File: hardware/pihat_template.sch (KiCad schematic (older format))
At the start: 29 parts, among them P1 CONN_01X02, P2 CONN_01X02, P3 Raspberry_Pi_+_Conn, U1 LM3489, U2 CAT24C32HU4I-GT3, U3 FDC5614P, U4 LM1117IMPX-ADJ

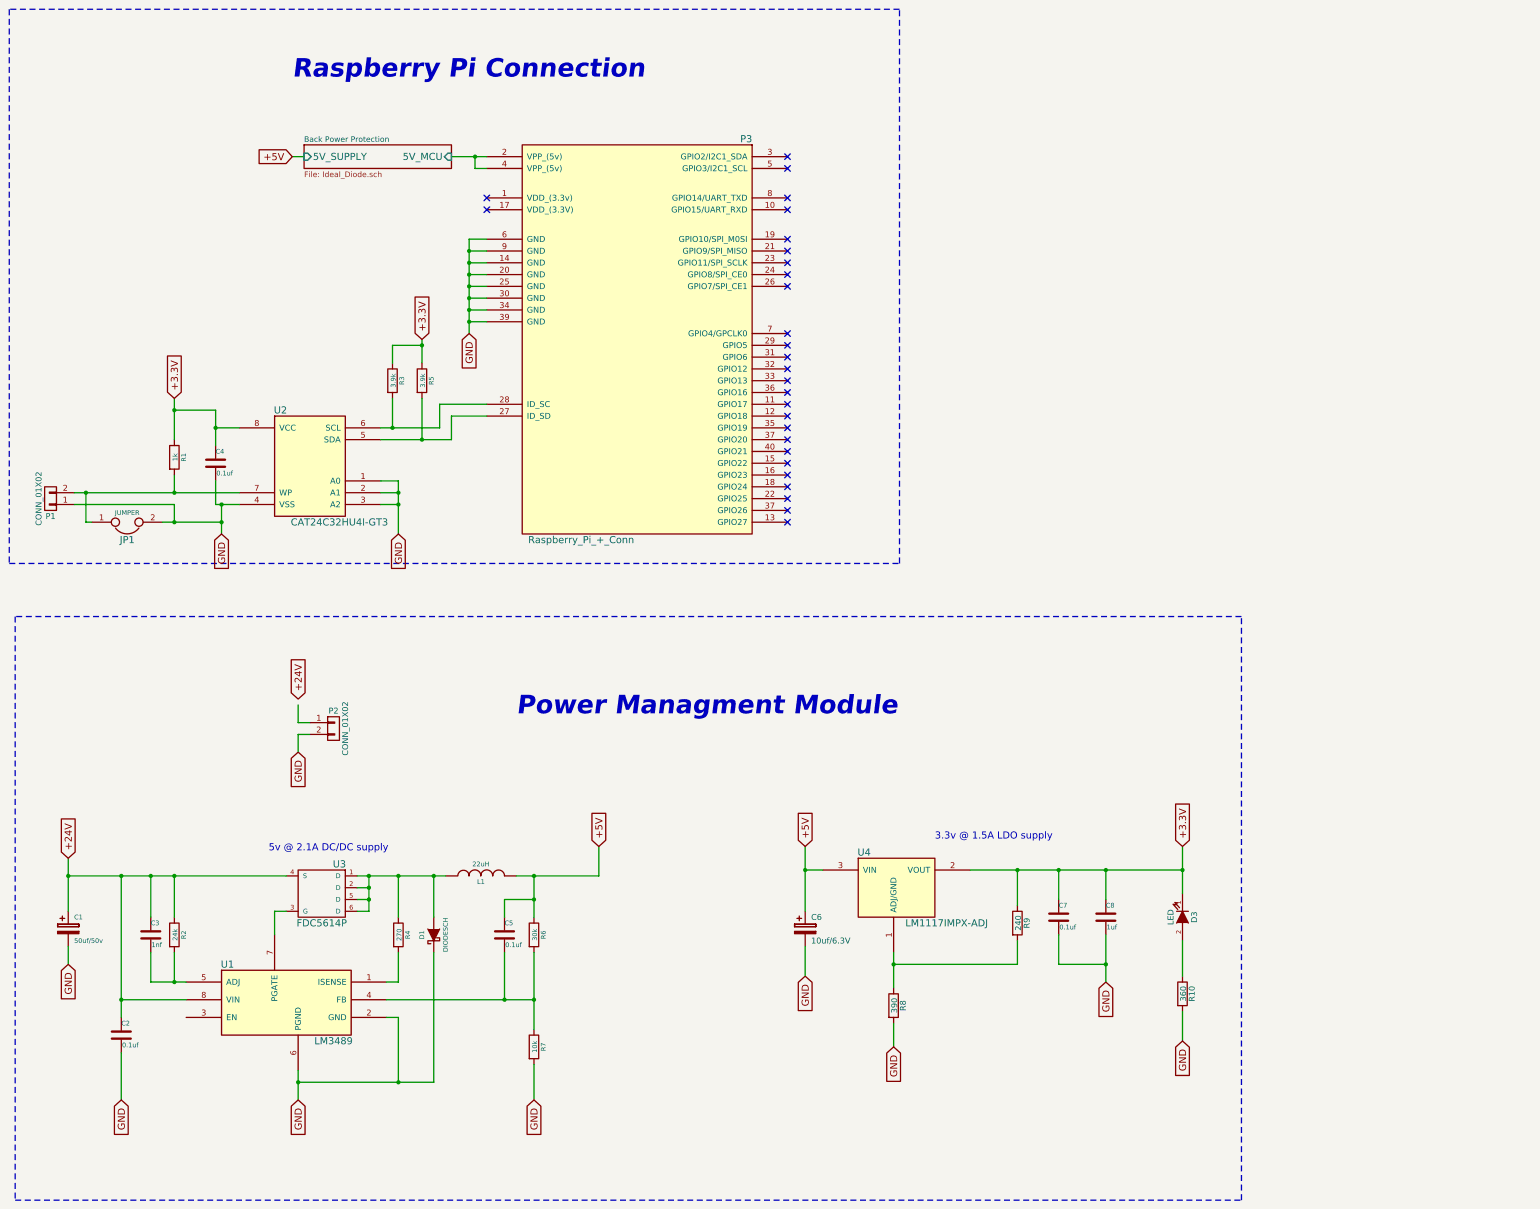
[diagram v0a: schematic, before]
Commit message: add PWR flag and fix electric check
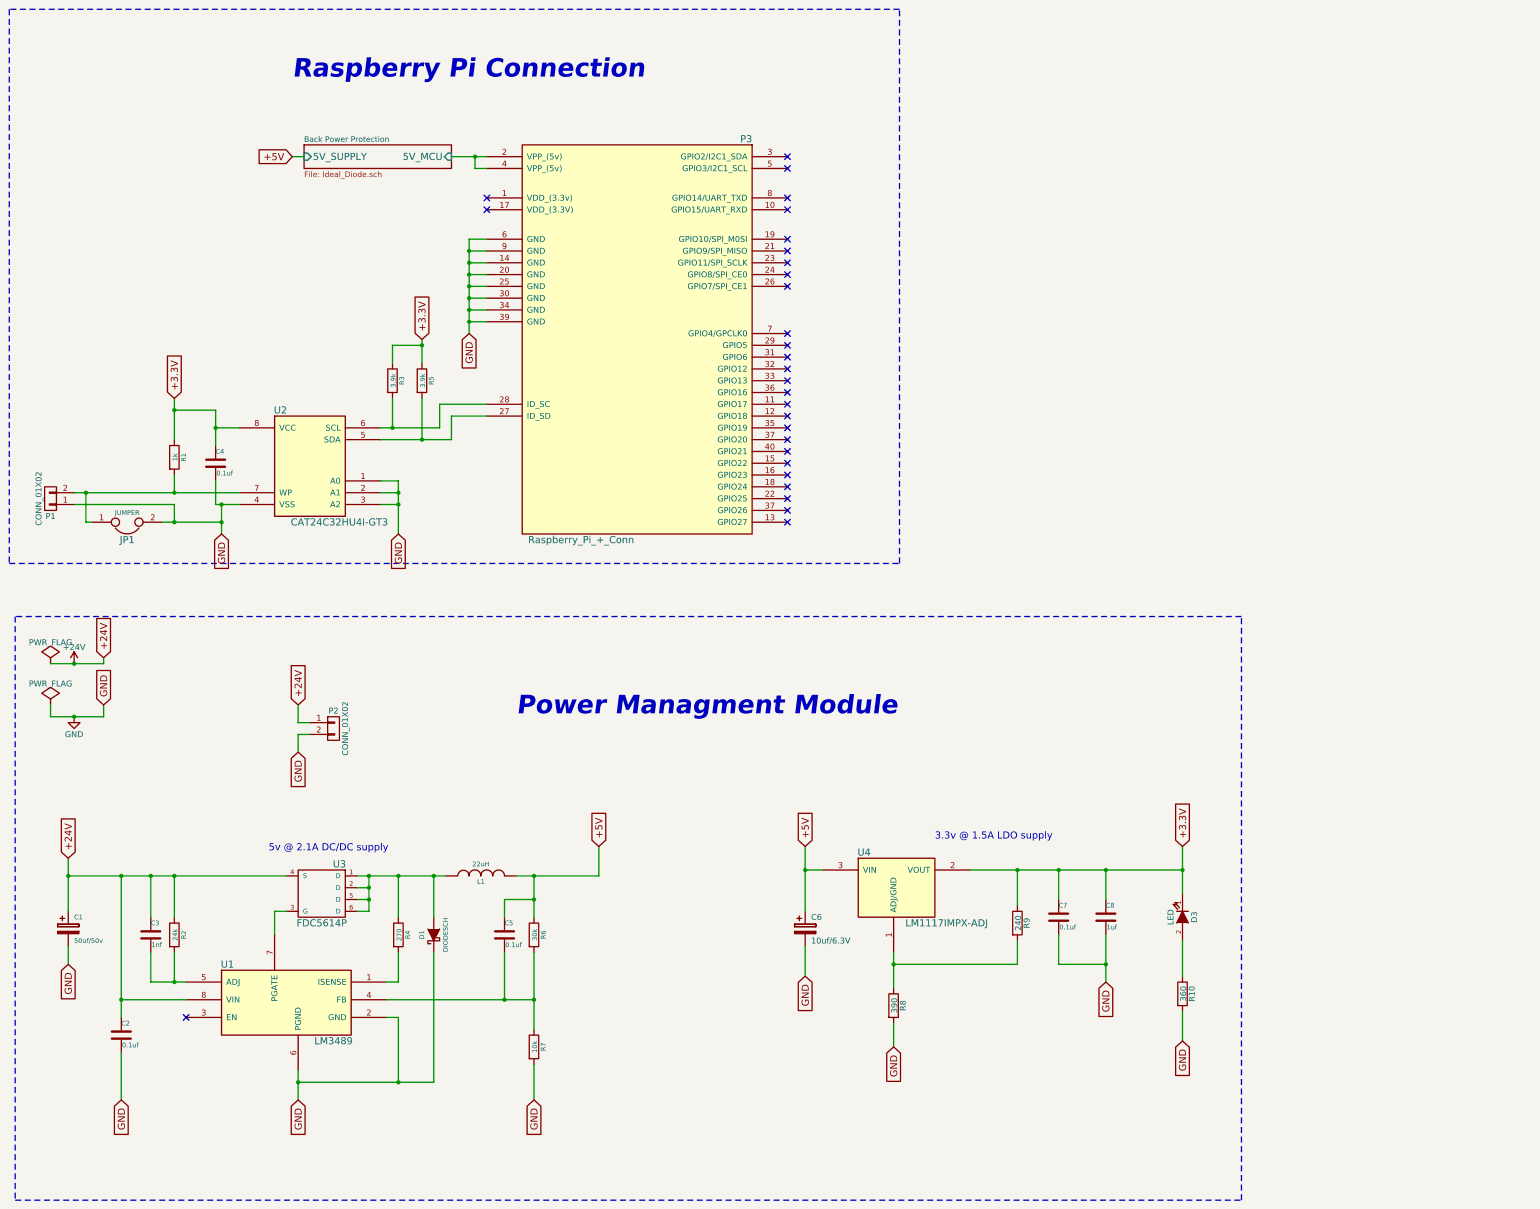
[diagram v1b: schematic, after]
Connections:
- net +24V: now also P2.1 (P1)
- no-connect marks 28 -> 29
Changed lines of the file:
@@
 	4100 3700 3850 3700
 Wire Wire Line
-	4100 3650 4100 3700
-Wire Wire Line
-	4100 3700 4100 3850
+	4100 3650 4100 3850
 Connection ~ 4100 4500
 Wire Wire Line
@@
 	3850 4150 3850 4400
 Wire Wire Line
-	3750 4500 4100 4500
-Wire Wire Line
-	4100 4500 4350 4500
+	3750 4500 4350 4500
 Wire Wire Line
 	4350 4500 4350 4300
@@
 	4250 4400 4250 4200
 Wire Wire Line
-	3750 4400 3850 4400
-Wire Wire Line
-	3850 4400 4250 4400
+	3750 4400 4250 4400
 Connection ~ 1250 4950
 Wire Wire Line
@@
 Connection ~ 2000 4950
 Wire Wire Line
-	2000 4800 2000 4950
-Wire Wire Line
-	1150 4950 1250 4950
-Wire Wire Line
-	1250 4950 2000 4950
-Wire Wire Line
-	2000 4950 2550 4950
+	2000 4950 2000 4800
+Wire Wire Line
+	1150 4950 2550 4950
 Connection ~ 2000 4250
 Wire Wire Line
 	2350 4250 2000 4250
 Wire Wire Line
-	2350 4250 2350 4400
-Wire Wire Line
-	2350 4400 2350 4550
+	2350 4250 2350 4550
 Wire Wire Line
 	2550 4400 2350 4400
 Wire Wire Line
-	2000 4150 2000 4250
-Wire Wire Line
-	2000 4250 2000 4500
+	2000 4150 2000 4500
 Connection ~ 2400 5200
 Wire Wire Line
-	1900 5200 2000 5200
-Wire Wire Line
-	2000 5200 2400 5200
-Wire Wire Line
-	2400 5050 2400 5200
-Wire Wire Line
-	2400 5200 2400 5300
-Wire Wire Line
-	2350 5050 2400 5050
-Wire Wire Line
-	2400 5050 2550 5050
+	1900 5200 2400 5200
+Wire Wire Line
+	2400 5050 2400 5300
+Wire Wire Line
+	2350 5050 2550 5050
 Connection ~ 3900 4950
 Wire Wire Line
@@
 	3750 4950 3900 4950
 Wire Wire Line
-	3900 4850 3900 4950
-Wire Wire Line
-	3900 4950 3900 5050
-Wire Wire Line
-	3900 5050 3900 5300
+	3900 4850 3900 5300
 Wire Wire Line
 	3750 5050 3900 5050
@@
 	4500 3500 4650 3500
 Wire Wire Line
-	4500 2800 4500 2900
-Wire Wire Line
-	4500 2900 4500 3000
-Wire Wire Line
-	4500 3000 4500 3100
-Wire Wire Line
-	4500 3100 4500 3200
-Wire Wire Line
-	4500 3200 4500 3300
-Wire Wire Line
-	4500 3300 4500 3400
-Wire Wire Line
-	4500 3400 4500 3500
-Wire Wire Line
-	4500 3500 4500 3600
+	4500 2800 4500 3600
 Wire Wire Line
 	4650 2800 4500 2800
@@
 Connection ~ 4500 2900
 Wire Wire Line
-	4350 2100 4550 2100
-Wire Wire Line
-	4550 2100 4650 2100
+	4350 2100 4650 2100
 Wire Wire Line
 	4650 2200 4550 2200
@@
 Connection ~ 2400 5050
 Wire Wire Line
-	1800 9100 2000 9100
-Wire Wire Line
-	2000 9100 2100 9100
+	1800 9100 2100 9100
 Wire Wire Line
 	2000 8850 2000 9100
@@
 	2000 8200 2000 8550
 Wire Wire Line
-	1100 8200 1550 8200
-Wire Wire Line
-	1550 8200 1800 8200
-Wire Wire Line
-	1800 8200 2000 8200
-Wire Wire Line
-	2000 8200 2950 8200
-Wire Wire Line
-	1550 8200 1550 9250
-Wire Wire Line
-	1550 9250 1550 9400
+	1100 8200 2950 8200
+Wire Wire Line
+	1550 8200 1550 9400
 Wire Wire Line
 	1550 9250 2100 9250
@@
 	1550 9700 1550 10100
 Wire Wire Line
-	3050 9850 3050 9950
-Wire Wire Line
-	3050 9950 3050 10100
+	3050 9850 3050 10100
 Wire Wire Line
 	3800 9400 3900 9400
@@
 	3900 9400 3900 9950
 Wire Wire Line
-	4200 9950 3900 9950
-Wire Wire Line
-	3900 9950 3050 9950
+	3050 9950 4200 9950
 Connection ~ 3050 9950
 Wire Wire Line
@@
 Connection ~ 2000 9100
 Wire Wire Line
-	1100 8050 1100 8200
-Wire Wire Line
-	1100 8200 1100 8500
+	1100 8050 1100 8500
 Connection ~ 1550 8200
 Wire Wire Line
@@
 	3900 8850 3900 9100
 Wire Wire Line
-	3800 9250 4800 9250
-Wire Wire Line
-	4800 9250 5050 9250
-Wire Wire Line
-	3550 8200 3650 8200
-Wire Wire Line
-	3650 8200 3900 8200
-Wire Wire Line
-	3900 8200 4200 8200
-Wire Wire Line
-	4200 8200 4300 8200
+	3800 9250 5050 9250
+Wire Wire Line
+	3550 8200 4300 8200
 Wire Wire Line
 	4200 8200 4200 8550
@@
 	5050 9800 5050 10100
 Wire Wire Line
-	5050 8850 5050 9250
-Wire Wire Line
-	5050 9250 5050 9500
+	5050 8850 5050 9500
 Connection ~ 5050 9250
 Wire Wire Line
-	5050 8200 5050 8400
-Wire Wire Line
-	5050 8400 5050 8550
-Wire Wire Line
-	4900 8200 5050 8200
-Wire Wire Line
-	5050 8200 5600 8200
+	5050 8200 5050 8550
+Wire Wire Line
+	4900 8200 5600 8200
 Wire Wire Line
 	4800 8400 4800 8550
@@
 Connection ~ 4800 9250
 Wire Wire Line
-	4200 8850 4200 9950
+	4200 9950 4200 8850
 Connection ~ 3900 9950
 Connection ~ 5050 8200
@@
 	3550 8300 3650 8300
 Wire Wire Line
-	3650 8200 3650 8300
-Wire Wire Line
-	3650 8300 3650 8400
-Wire Wire Line
-	3650 8400 3650 8500
+	3650 8200 3650 8500
 Connection ~ 3650 8200
 Wire Wire Line
@@
 Connection ~ 1100 8200
 Wire Wire Line
-	7350 7950 7350 8150
-Wire Wire Line
-	7350 8150 7350 8500
+	7350 7950 7350 8500
 Connection ~ 7350 8150
 Wire Wire Line
-	8750 8150 9150 8150
-Wire Wire Line
-	9150 8150 9500 8150
-Wire Wire Line
-	9500 8150 9900 8150
-Wire Wire Line
-	9900 8150 10550 8150
+	8750 8150 10550 8150
 Wire Wire Line
 	9150 8150 9150 8450
 Wire Wire Line
-	8100 8850 8100 8950
-Wire Wire Line
-	8100 8950 8100 9150
+	8100 8850 8100 9150
 Wire Wire Line
 	9150 8750 9150 8950
@@
 	9150 8950 8100 8950
 Wire Wire Line
-	9900 8700 9900 8950
-Wire Wire Line
-	9900 8950 9900 9100
+	9900 8700 9900 9100
 Wire Wire Line
 	9500 8950 9900 8950
 Connection ~ 9900 8950
 Wire Wire Line
-	10550 7950 10550 8150
-Wire Wire Line
-	10550 8150 10550 8350
+	10550 7950 10550 8350
 Connection ~ 9900 8150
 Wire Wire Line
@@
 Text GLabel 1100 8050 1    60   Input ~ 0
 +24V
-Text GLabel 3050 6700 1    60   Input ~ 0
+Text GLabel 3050 6750 1    60   Input ~ 0
 +24V
 Text GLabel 10550 7950 1    60   Input ~ 0
@@
 Text GLabel 3000 2100 0    60   Input ~ 0
 +5V
+$Comp
+L PWR_FLAG #FLG01
+U 1 1 5A0F8FE9
+P 950 6400
+F 0 "#FLG01" H 950 6495 50  0001 C CNN
+F 1 "PWR_FLAG" H 950 6580 50  0000 C CNN
+F 2 "" H 950 6400 50  0000 C CNN
+F 3 "" H 950 6400 50  0000 C CNN
+	1    950  6400
+	1    0    0    -1
+$EndComp
+Text GLabel 1400 6350 1    60   Input ~ 0
++24V
+Wire Wire Line
+	950  6400 1400 6400
+Connection ~ 1150 6400
+Wire Wire Line
+	1400 6400 1400 6350
+$Comp
+L +24V #PWR02
+U 1 1 5A0FA5E7
+P 1150 6400
+F 0 "#PWR02" H 1150 6250 50  0001 C CNN
+F 1 "+24V" H 1150 6540 50  0000 C CNN
+F 2 "" H 1150 6400 50  0000 C CNN
+F 3 "" H 1150 6400 50  0000 C CNN
+	1    1150 6400
+	1    0    0    -1
+$EndComp
+$Comp
+L PWR_FLAG #FLG03
+U 1 1 5A0FA894
+P 950 6750
+F 0 "#FLG03" H 950 6845 50  0001 C CNN
+F 1 "PWR_FLAG" H 950 6930 50  0000 C CNN
+F 2 "" H 950 6750 50  0000 C CNN
+F 3 "" H 950 6750 50  0000 C CNN
+	1    950  6750
+	1    0    0    -1
+$EndComp
+Text GLabel 1400 6750 1    60   Input ~ 0
+GND
+$Comp
+L GND #PWR04
+U 1 1 5A0FAA8E
+P 1150 6850
+F 0 "#PWR04" H 1150 6600 50  0001 C CNN
+F 1 "GND" H 1150 6700 50  0000 C CNN
+F 2 "" H 1150 6850 50  0000 C CNN
+F 3 "" H 1150 6850 50  0000 C CNN
+	1    1150 6850
+	1    0    0    -1
+$EndComp
+Wire Wire Line
+	950  6850 1400 6850
+Wire Wire Line
+	1400 6850 1400 6750
+Wire Wire Line
+	950  6750 950  6850
+Connection ~ 1150 6850
+NoConn ~ 2100 9400
 $EndSCHEMATC

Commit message: change resistors form factor to 0805
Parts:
- R1, R10, R2, R3, R4, R5, R6, R7, R8, R9: footprint project:r_0402 -> Resistors_SMD:R_0805
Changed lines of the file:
@@
 F 0 "R1" V 2080 4650 40  0000 C CNN
 F 1 "1k" V 2007 4651 40  0000 C CNN
-F 2 "project:r_0402" V 1930 4650 30  0001 C CNN
+F 2 "Resistors_SMD:R_0805" V 1930 4650 30  0001 C CNN
 F 3 "" H 2000 4650 30  0000 C CNN
 F 4 "754-RR0510P-102D" V 2000 4650 60  0001 C CNN "Mouser Part No."
@@
 F 0 "R3" V 3930 4000 40  0000 C CNN
 F 1 "3.9k" V 3857 4001 40  0000 C CNN
-F 2 "project:r_0402" V 3780 4000 30  0001 C CNN
+F 2 "Resistors_SMD:R_0805" V 3780 4000 30  0001 C CNN
 F 3 "" H 3850 4000 30  0000 C CNN
 F 4 "71-CRCW04023K90FKED" V 3850 4000 60  0001 C CNN "Mouser Part No."
@@
 F 0 "R5" V 4180 4000 40  0000 C CNN
 F 1 "3.9k" V 4107 4001 40  0000 C CNN
-F 2 "project:r_0402" V 4030 4000 30  0001 C CNN
+F 2 "Resistors_SMD:R_0805" V 4030 4000 30  0001 C CNN
 F 3 "" H 4100 4000 30  0000 C CNN
 F 4 "71-CRCW04023K90FKED" V 4100 4000 60  0001 C CNN "Mouser Part No."
@@
 F 0 "R2" V 2080 8700 40  0000 C CNN
 F 1 "24k" V 2007 8701 40  0000 C CNN
-F 2 "project:r_0402" V 1930 8700 30  0001 C CNN
+F 2 "Resistors_SMD:R_0805" V 1930 8700 30  0001 C CNN
 F 3 "" H 2000 8700 30  0000 C CNN
 F 4 "71-CRCW0402-24K-E3" V 2000 8700 60  0001 C CNN "Mouser Part No."
@@
 F 0 "R4" V 3980 8700 40  0000 C CNN
 F 1 "270" V 3907 8701 40  0000 C CNN
-F 2 "project:r_0402" V 3830 8700 30  0001 C CNN
+F 2 "Resistors_SMD:R_0805" V 3830 8700 30  0001 C CNN
 F 3 "" H 3900 8700 30  0000 C CNN
 F 4 "667-ERJ-P6WJ271V" V 3900 8700 60  0001 C CNN "Mouser Part No."
@@
 F 0 "R6" V 5130 8700 40  0000 C CNN
 F 1 "30k" V 5057 8701 40  0000 C CNN
-F 2 "project:r_0402" V 4980 8700 30  0001 C CNN
+F 2 "Resistors_SMD:R_0805" V 4980 8700 30  0001 C CNN
 F 3 "" H 5050 8700 30  0000 C CNN
 F 4 "594-MCT06030C3002FP5" V 5050 8700 60  0001 C CNN "Mouser Part No."
@@
 F 0 "R7" V 5130 9650 40  0000 C CNN
 F 1 "10k" V 5057 9651 40  0000 C CNN
-F 2 "project:r_0402" V 4980 9650 30  0001 C CNN
+F 2 "Resistors_SMD:R_0805" V 4980 9650 30  0001 C CNN
 F 3 "" H 5050 9650 30  0000 C CNN
 F 4 "71-CRCW0603-10K-E3" V 5050 9650 60  0001 C CNN "Mouser Part No."
@@
 F 0 "R8" V 8180 9300 50  0000 C CNN
 F 1 "390" V 8107 9301 50  0000 C CNN
-F 2 "project:r_0402" V 8030 9300 30  0001 C CNN
+F 2 "Resistors_SMD:R_0805" V 8030 9300 30  0001 C CNN
 F 3 "" H 8100 9300 30  0000 C CNN
 F 4 "594-MCT06030C3900FP5" V 8100 9300 60  0001 C CNN "Mouser Part No."
@@
 F 0 "R9" V 9230 8600 50  0000 C CNN
 F 1 "240" V 9157 8601 50  0000 C CNN
-F 2 "project:r_0402" V 9080 8600 30  0001 C CNN
+F 2 "Resistors_SMD:R_0805" V 9080 8600 30  0001 C CNN
 F 3 "" H 9150 8600 30  0000 C CNN
 F 4 "754-RR0816P-241D" V 9150 8600 60  0001 C CNN "Mouser Part No."
@@
 F 0 "R10" V 10630 9200 50  0000 C CNN
 F 1 "360" V 10557 9201 50  0000 C CNN
-F 2 "project:r_0402" V 10480 9200 30  0001 C CNN
+F 2 "Resistors_SMD:R_0805" V 10480 9200 30  0001 C CNN
 F 3 "" H 10550 9200 30  0000 C CNN
 F 4 "71-CRCW0603316RFKEB" V 10550 9200 60  0001 C CNN "Mouser Part No."

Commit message: change some resistors and capacitors form factor to 0805
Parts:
- C2, C3, C4, C5, C7, C8: footprint project:c_0402 -> Capacitors_SMD:C_0805
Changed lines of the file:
@@
 F 0 "C2" H 1550 9650 40  0000 L CNN
 F 1 "0.1uf" H 1556 9465 40  0000 L CNN
-F 2 "project:c_0402" H 1588 9400 30  0001 C CNN
+F 2 "Capacitors_SMD:C_0805" H 1588 9400 30  0001 C CNN
 F 3 "" H 1550 9550 60  0000 C CNN
 F 4 "810-C1005X5R1H104K" H 1550 9550 60  0001 C CNN "Mouser Part No."
@@
 F 0 "C3" H 1800 8800 40  0000 L CNN
 F 1 "1nf" H 1806 8615 40  0000 L CNN
-F 2 "project:c_0402" H 1838 8550 30  0001 C CNN
+F 2 "Capacitors_SMD:C_0805" H 1838 8550 30  0001 C CNN
 F 3 "" H 1800 8700 60  0000 C CNN
 F 4 "810-C1005C0G2A102J5C" H 1800 8700 60  0001 C CNN "Mouser Part No."
@@
 F 0 "C5" H 4800 8800 40  0000 L CNN
 F 1 "0.1uf" H 4806 8615 40  0000 L CNN
-F 2 "project:c_0402" H 4838 8550 30  0001 C CNN
+F 2 "Capacitors_SMD:C_0805" H 4838 8550 30  0001 C CNN
 F 3 "" H 4800 8700 60  0000 C CNN
 F 4 "810-C1005X5R1H104K" H 4800 8700 60  0001 C CNN "Mouser Part No."
@@
 F 0 "C7" H 9500 8650 40  0000 L CNN
 F 1 "0.1uf" H 9506 8465 40  0000 L CNN
-F 2 "project:c_0402" H 9538 8400 30  0001 C CNN
+F 2 "Capacitors_SMD:C_0805" H 9538 8400 30  0001 C CNN
 F 3 "" H 9500 8550 60  0000 C CNN
 F 4 "810-C1005X5R1H104K" H 9500 8550 60  0001 C CNN "Mouser Part No."
@@
 F 0 "C4" H 2350 4800 40  0000 L CNN
 F 1 "0.1uf" H 2356 4615 40  0000 L CNN
-F 2 "project:c_0402" H 2388 4550 30  0001 C CNN
+F 2 "Capacitors_SMD:C_0805" H 2388 4550 30  0001 C CNN
 F 3 "" H 2350 4700 60  0000 C CNN
 F 4 "810-C1005X5R1H104K" H 2350 4700 60  0001 C CNN "Mouser Part No."
@@
 F 0 "C8" H 9900 8650 40  0000 L CNN
 F 1 "1uf" H 9906 8465 40  0000 L CNN
-F 2 "project:c_0402" H 9938 8400 30  0001 C CNN
+F 2 "Capacitors_SMD:C_0805" H 9938 8400 30  0001 C CNN
 F 3 "" H 9900 8550 60  0000 C CNN
 F 4 "810-C1005X5R1H104K" H 9900 8550 60  0001 C CNN "Mouser Part No."

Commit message: add new eeprom reference
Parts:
- U2: value CAT24C32HU4I-GT3 -> CAT24C04WI-GT3; footprint project:tssop-8 -> project:CAT24C04WI-GT3; Farnell Part No. 2463727 -> 2463704
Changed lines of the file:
@@
 P 3000 4400
 F 0 "U2" H 2900 4550 60  0000 C CNN
-F 1 "CAT24C32HU4I-GT3" H 3400 3600 60  0000 C CNN
-F 2 "project:tssop-8" H 3000 4400 60  0001 C CNN
+F 1 "CAT24C04WI-GT3 " H 3400 3600 60  0000 C CNN
+F 2 "project:CAT24C04WI-GT3" H 3000 4400 60  0001 C CNN
 F 3 "" H 3000 4400 60  0000 C CNN
 F 4 "698-CAT24C32YI-GT3" H 3000 4400 60  0001 C CNN "Mouser Part No."
-F 5 "2463727" H 3000 4400 60  0001 C CNN "Farnell Part No."
+F 5 "2463704" H 3000 4400 60  0001 C CNN "Farnell Part No."
 	1    3000 4400
 	1    0    0    -1
